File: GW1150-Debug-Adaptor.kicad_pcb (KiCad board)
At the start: 2 copper layers, 44.6 x 13.2 mm, 6 parts, among them J1 SW_SPDT, J2 Conn_02x03_Counter_Clockwise, J3 Conn_02x03_Counter_Clockwise, J4 SW_SPDT, J5 Conn_01x06

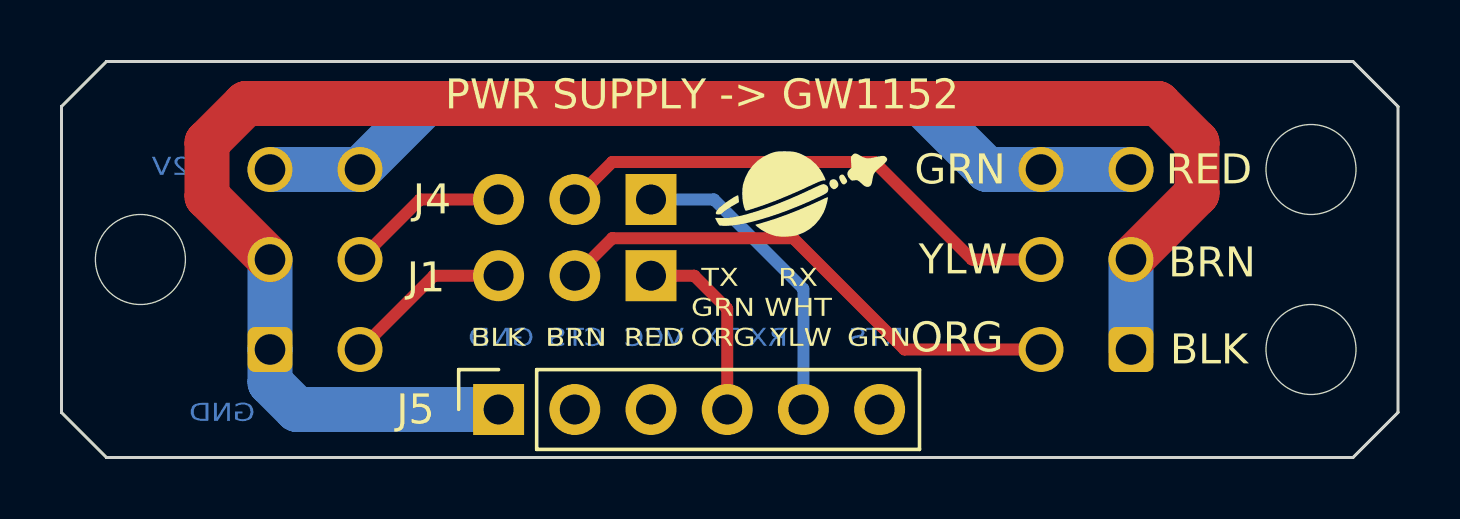
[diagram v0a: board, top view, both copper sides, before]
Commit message: v1.0 changes after building initial units. Enlarged drill holes for cable whip. Added shunts across the jumpers, for default use. miscellaneous labeling.
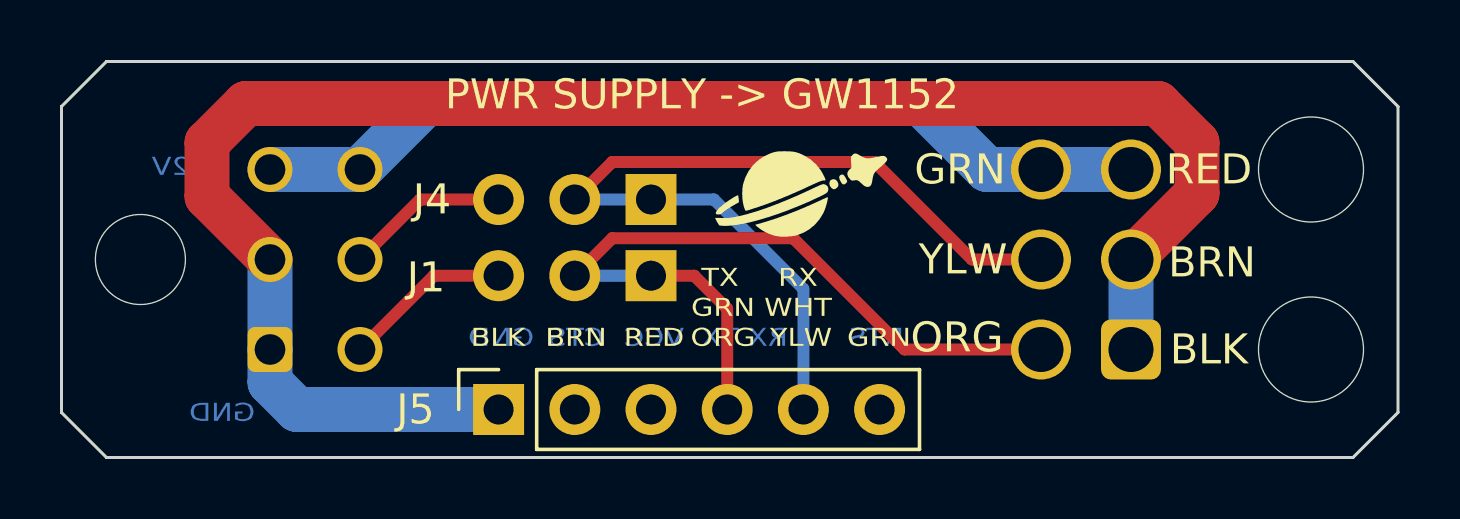
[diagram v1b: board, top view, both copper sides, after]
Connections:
- J1 pad 1: /TxD_FTDI -> /RxD_ROUTER
- J4 pad 1: /RxD_FTDI -> /TxD_ROUTER
- J5 pad 4: /TxD_FTDI -> /RxD_ROUTER
- J5 pad 5: /RxD_FTDI -> /TxD_ROUTER
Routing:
- net /TxD_ROUTER: track 17.4 -> 30.3 mm
- net /RxD_FTDI: track 10.3 -> 0.00 mm
- net /RxD_ROUTER: track 17.6 -> 26.5 mm
- net /TxD_FTDI: track 6.36 -> 0.00 mm
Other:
- board text added: "2x Nylon Tie Wrap"
- board text added: "All color labelings are typical. Actual may vary. Please check."
